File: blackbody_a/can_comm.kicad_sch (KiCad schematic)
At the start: 8 parts, among them U2 TCAN337DCNR

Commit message: layout updates
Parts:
- C9: Manufacturer_Part_Number (none) -> 80-C0805C104M5RACTU; Mouser Part Number (none) -> 80-C0805C104M5RACTU; PN (none) -> C0805C104M5RACTU
- D1: Mouser Part Number 652-CDSOT23-T24CAN -> 637-BAS70-04; PN (none) -> BAS7004
- D7: Manufacturer_Part_Number (none) -> 604-APTD2012LCGCK; PN (none) -> APTD2012LCGCK
- R16: Mouser Part Number (none) -> 603-RT0805FRE0710KL; PN (none) -> CRCW080510K0FKEA
- R18: value 2.2k -> 10k; PN (none) -> CRCW080510K0FKEA
- R4: Mouser Part Number (none) -> 71-CRCW0805120RFKEA; PN (none) -> CRCW0805120RFKEA
- U2: Mouser Part Number (none) -> 652-CDSOT23-T24CAN; PN (none) -> CDSOT23-T24CAN
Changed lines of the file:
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@@
+			)
+		)
+		(property "Mouser Part Number" "603-RT0805FRE0710KL"
+			(at 191.77 74.93 0)
+			(effects
+				(font
+					(size 1.27 1.27)
+				)
+			)
+		)
+		(property "PN" "CRCW080510K0FKEA"
+			(at 191.77 74.93 0)
+			(effects
+				(font
+					(size 1.27 1.27)
+				)
 			)
 		)
@@
 			)
 		)
-		(property "PN" ""
+		(property "PN" "APTD2012LCGCK"
 			(at 191.77 83.82 0)
 			(effects
@@
 				)
 				(hide yes)
+			)
+		)
+		(property "Manufacturer_Part_Number" "604-APTD2012LCGCK"
+			(at 191.77 83.82 0)
+			(effects
+				(font
+					(size 1.27 1.27)
+				)
 			)
 		)
@@
 			)
 		)
-		(property "Mouser Part Number" "652-CDSOT23-T24CAN"
+		(property "Mouser Part Number" "637-BAS70-04"
 			(at 171.45 599.06 0)
 			(effects
@@
 				(justify left top)
 				(hide yes)
+			)
+		)
+		(property "PN" "BAS7004"
+			(at 152.4 104.14 0)
+			(effects
+				(font
+					(size 1.27 1.27)
+				)
 			)
 		)
@@
 			)
 		)
+		(property "Mouser Part Number" "71-CRCW0805120RFKEA"
+			(at 140.97 99.06 0)
+			(effects
+				(font
+					(size 1.27 1.27)
+				)
+			)
+		)
+		(property "PN" "CRCW0805120RFKEA"
+			(at 140.97 99.06 0)
+			(effects
+				(font
+					(size 1.27 1.27)
+				)
+			)
+		)
 		(pin "2"
 		)
@@
 			)
 		)
+		(property "Mouser Part Number" "652-CDSOT23-T24CAN"
+			(at 113.03 93.98 0)
+			(effects
+				(font
+					(size 1.27 1.27)
+				)
+			)
+		)
+		(property "PN" "CDSOT23-T24CAN"
+			(at 113.03 93.98 0)
+			(effects
+				(font
+					(size 1.27 1.27)
+				)
+			)
+		)
 		(pin "8"
 		)
@@
 			)
 		)
-		(property "Value" "2.2k"
+		(property "Value" "10k"
 			(at 133.858 83.693 0)
 			(effects
@@
 			)
 		)
-		(property "PN" ""
+		(property "PN" "CRCW080510K0FKEA"
 			(at 132.08 82.55 0)
 			(effects
@@
 			)
 		)
+		(property "Manufacturer_Part_Number" "80-C0805C104M5RACTU"
+			(at 81.28 91.44 0)
+			(effects
+				(font
+					(size 1.27 1.27)
+				)
+			)
+		)
+		(property "Mouser Part Number" "80-C0805C104M5RACTU"
+			(at 81.28 91.44 0)
+			(effects
+				(font
+					(size 1.27 1.27)
+				)
+			)
+		)
+		(property "PN" "C0805C104M5RACTU"
+			(at 81.28 91.44 0)
+			(effects
+				(font
+					(size 1.27 1.27)
+				)
+			)
+		)

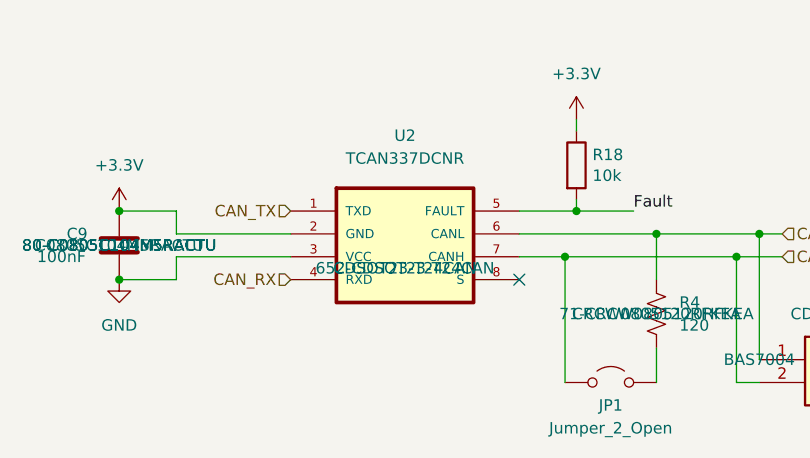
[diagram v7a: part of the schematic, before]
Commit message: fixed footprint issue
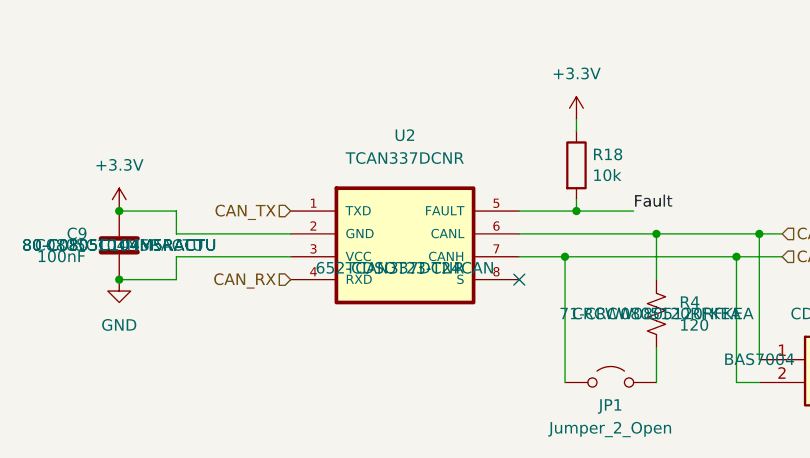
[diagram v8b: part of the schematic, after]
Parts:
- U2: footprint UTSVT_ICs:SOP65P640X120-16N -> blackbody_a:SOT65P280X145-8N; PN CDSOT23-T24CAN -> TCAN337DCNR
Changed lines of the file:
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@@
 			)
 		)
-		(property "Footprint" "UTSVT_ICs:SOP65P640X120-16N"
+		(property "Footprint" "blackbody_a:SOT65P280X145-8N"
 			(at 115.57 95.25 0)
 			(effects
@@
 			)
 		)
-		(property "PN" "CDSOT23-T24CAN"
+		(property "PN" "TCAN337DCNR"
 			(at 113.03 93.98 0)
 			(effects
